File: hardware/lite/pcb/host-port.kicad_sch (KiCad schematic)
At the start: 16 parts, among them J901 1054500101, U901 TPD4E02B04DQAR, U902 TPD4E02B04DQAR, U903 HD3SS3212IRKSR, U904 TPD6S300ARUKR, U905 FUSB302BMPX

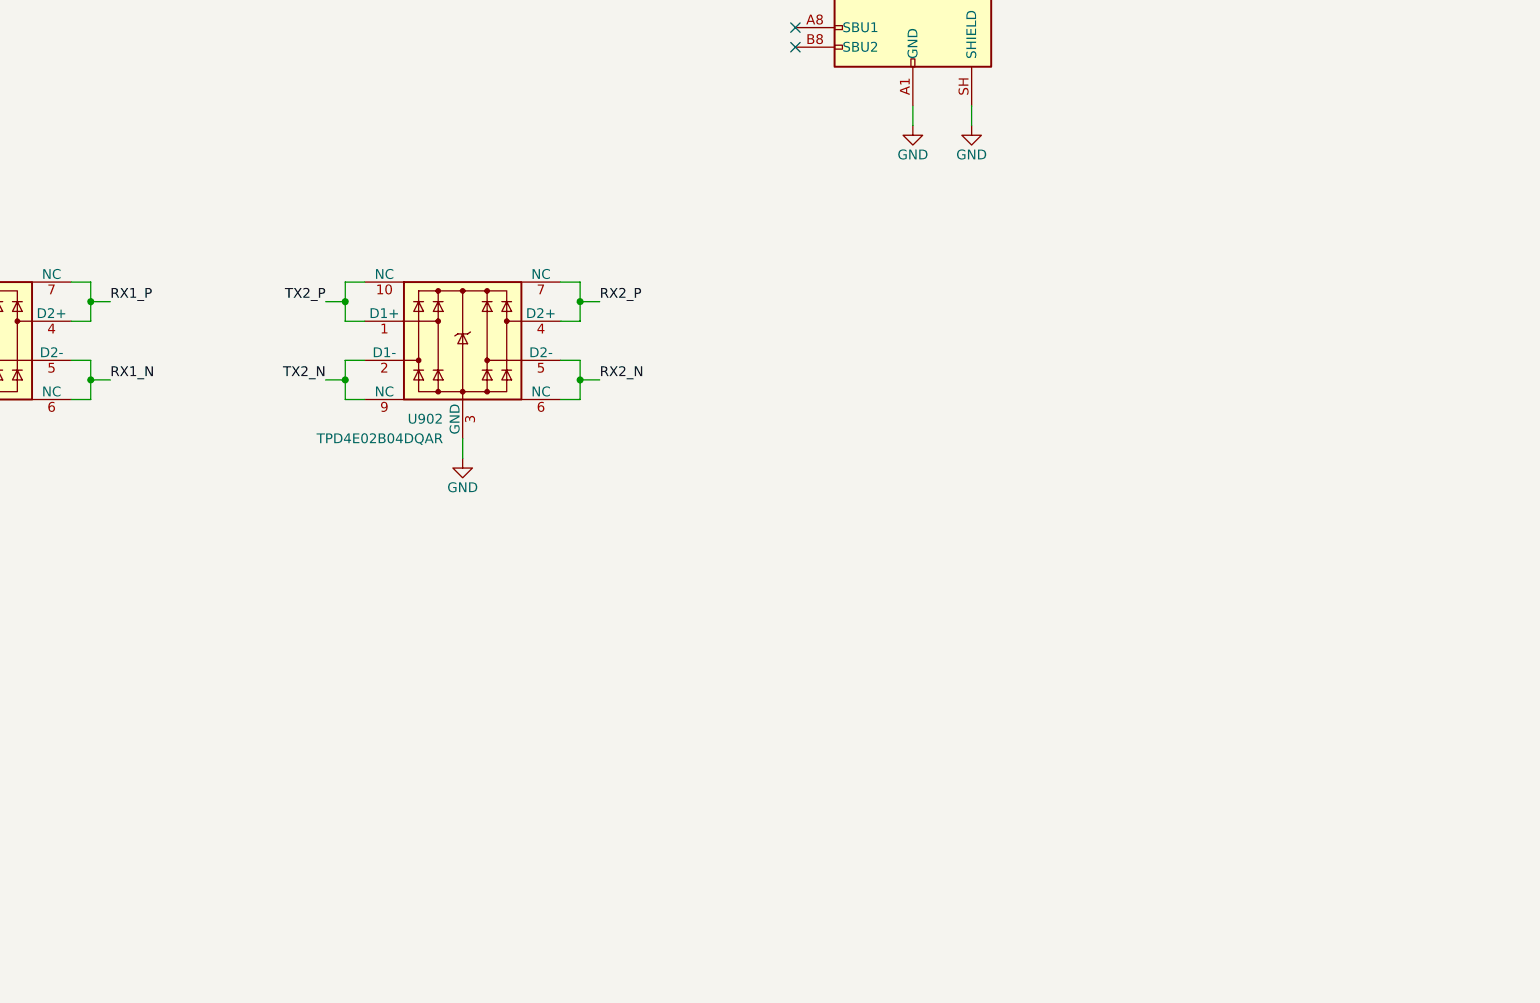
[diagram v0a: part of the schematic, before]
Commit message: feat(hardware): share brick power across ports and add CM5 link
A connected PD supply now runs the logic through its own buck and feeds
one TPS55288 buck-boost stage per port, so the contract is shared as
5-20 V at up to 5 A per port. The hub's VBUS detect becomes an OR gate,
a host-select mux lets a CM5 side board drive the hub over a 24-pin ZIF
link, and a CM5 variant joins Hub and HubPD.

The board is synced to the schematic and its old routing removed; the
new parts wait below the outline for placement.
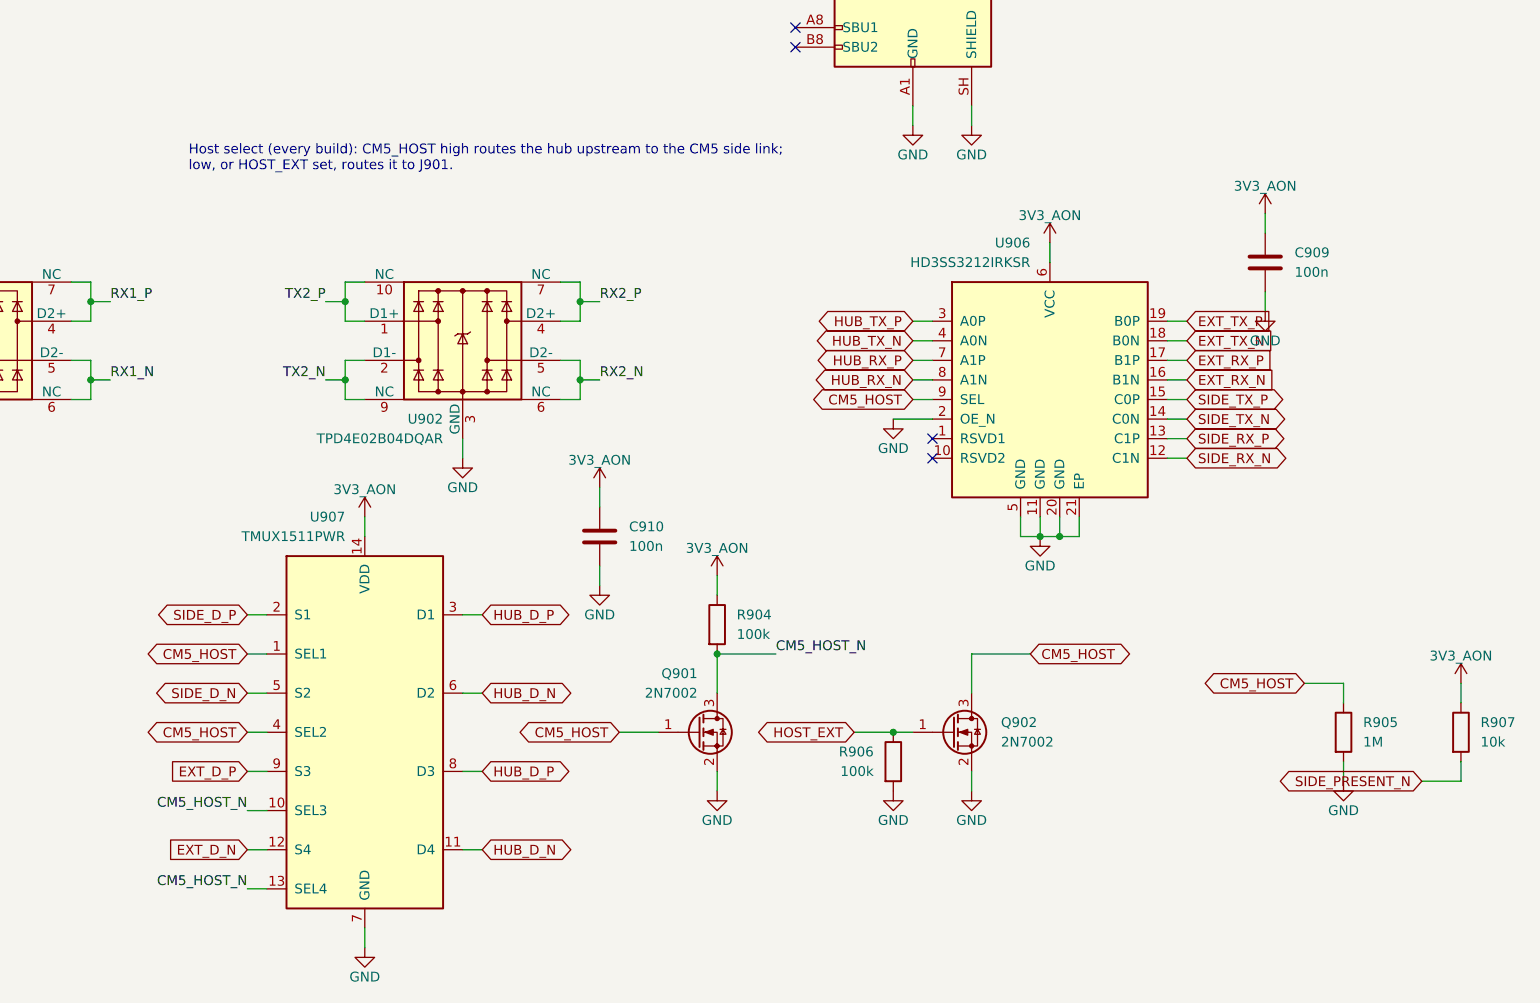
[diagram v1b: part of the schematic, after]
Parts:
- added C909, C910: 100n, Capacitor_SMD:C_0402_1005Metric, symbol Device:C
- added Q901, Q902: 2N7002, Package_TO_SOT_SMD:SOT-23, symbol Transistor_FET:2N7002
- added R904, R906: 100k, Resistor_SMD:R_0402_1005Metric, symbol Device:R
- added R905: 1M, Resistor_SMD:R_0402_1005Metric, symbol Device:R
- added R907: 10k, Resistor_SMD:R_0402_1005Metric, symbol Device:R
- added U906: HD3SS3212IRKSR, Package_DFN_QFN:DHVQFN-20-1EP_2.5x4.5mm_P0.5mm_EP1x3mm, symbol Iasis:HD3SS3212IRKSR
- added U907: TMUX1511PWR, Package_SO:TSSOP-14_4.4x5mm_P0.65mm, symbol Iasis:TMUX1511PWR
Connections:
- net 3V3_AON: now also C909.1, C910.1, R904.1, R907.1, U906.6 (VCC), U907.14 (VDD)
- net EXT_D_N: now also U907.12 (S4)
- net EXT_D_P: now also U907.9 (S3)
- net EXT_RX_N: now also U906.16 (B1N)
- net EXT_RX_P: now also U906.17 (B1P)
- net EXT_TX_N: now also U906.18 (B0N)
- net EXT_TX_P: now also U906.19 (B0P)
- net GND: now also C909.2, C910.2, Q901.2 (S), Q902.2 (S), R905.2, R906.2, U906.11 (GND), U906.2 (OE_N), U906.20 (GND), U906.21 (EP), U906.5 (GND), U907.7 (GND)
- new net CM5_HOST: Q901.1 (G), Q902.3 (D), R905.1, U906.9 (SEL), U907.1 (SEL1), U907.4 (SEL2)
- new net CM5_HOST_N: Q901.3 (D), R904.2, U907.10 (SEL3), U907.13 (SEL4)
- new net HOST_EXT: Q902.1 (G), R906.1
- new net HUB_D_N: U907.11 (D4), U907.6 (D2)
- new net HUB_D_P: U907.3 (D1), U907.8 (D3)
- new net HUB_RX_N: U906.8 (A1N)
- new net HUB_RX_P: U906.7 (A1P)
- new net HUB_TX_N: U906.4 (A0N)
- new net HUB_TX_P: U906.3 (A0P)
- new net SIDE_D_N: U907.5 (S2)
- new net SIDE_D_P: U907.2 (S1)
- new net SIDE_PRESENT_N: R907.2
- new net SIDE_RX_N: U906.12 (C1N)
- new net SIDE_RX_P: U906.13 (C1P)
- new net SIDE_TX_N: U906.14 (C0N)
- new net SIDE_TX_P: U906.15 (C0P)
- no-connect marks 5 -> 7
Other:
- note added: "Host select (every build): CM5_HOST high routes the hub upstream to the CM5 side link; low, or HOST_EXT set, routes it to J901."

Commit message: feat(hardware): use smaller mux, I2C switch, 595 and button packages
The TMUX1511s move to UQFN-16 (RSV), the TCA9548A to VQFN-24 (RGE),
the 74HC595s to TSSOP-16 and the BOOTSEL and RESET buttons to the
Omron B3U, which frees about 300 mm2 of the middle band. The case
button keeps the PTS645.
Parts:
- U907: value TMUX1511PWR -> TMUX1511RSVR; footprint Package_SO:TSSOP-14_4.4x5mm_P0.65mm -> Package_DFN_QFN:UQFN-16_1.8x2.6mm_P0.4mm; symbol Iasis:TMUX1511PWR -> Iasis:TMUX1511RSVR; LCSC C2866750 -> C2673275; MPN TMUX1511PWR -> TMUX1511RSVR
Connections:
- net 3V3_AON: now also U907.16 (VDD); no longer U907.14 (VDD)
- net CM5_HOST_N: now also U907.11 (SEL3), U907.15 (SEL4); no longer U907.10 (SEL3), U907.13 (SEL4)
- net EXT_D_N: now also U907.14 (S4); no longer U907.12 (S4)
- net EXT_D_P: now also U907.10 (S3); no longer U907.9 (S3)
- net GND: now also U907.8 (GND); no longer U907.7 (GND)
- net HUB_D_N: now also U907.13 (D4); no longer U907.11 (D4)
- net HUB_D_P: now also U907.9 (D3); no longer U907.8 (D3)
- no-connect marks 7 -> 9
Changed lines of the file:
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@@
 	)
 	(no_connect
+		(at 266.7 251.46)
+	)
+	(no_connect
+		(at 266.7 210.82)
+	)
+	(no_connect
 		(at 241.3 88.9)
 	)
@@
 	)
 	(symbol
-		(lib_id "Iasis:TMUX1511PWR")
+		(lib_id "Iasis:TMUX1511RSVR")
 		(at 254 231.14 0)
 		(unit 1)
@@
 			)
 		)
-		(property "Value" "TMUX1511PWR"
+		(property "Value" "TMUX1511RSVR"
 			(at 251.46 205.74 0)
 			(show_name no)
@@
 			)
 		)
-		(property "Footprint" "Package_SO:TSSOP-14_4.4x5mm_P0.65mm"
+		(property "Footprint" "Package_DFN_QFN:UQFN-16_1.8x2.6mm_P0.4mm"
 			(at 254 231.14 0)
 			(hide yes)
@@
 			)
 		)
-		(property "LCSC" "C2866750"
+		(property "LCSC" "C2673275"
 			(at 254 231.14 0)
 			(hide yes)
@@
 			)
 		)
-		(property "MPN" "TMUX1511PWR"
+		(property "MPN" "TMUX1511RSVR"
 			(at 254 231.14 0)
 			(hide yes)
@@
 		(pin "6"
 		)
-		(pin "7"
-		)
 		(pin "8"
 		)
@@
 		(pin "11"
 		)
-		(pin "12"
-		)
 		(pin "13"
 		)
 		(pin "14"
 		)
+		(pin "15"
+		)
+		(pin "16"
+		)
+		(pin "7"
+		)
+		(pin "12"
+		)
 		(instances

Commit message: fix(hardware): put the hub and side-link lanes in USB_90
The hub upstream and CM5 side-link nets (HUB_ and SIDE_ TX, RX and D)
were left in the default class when the side link was added. A rule
lets the TMUX1511's corner pads keep their 0.15 mm package spacing
inside the class clearance.

U907 now carries D- on channel 1 and D+ on channel 2, the reverse of
channels 3 and 4, so each HUB_D net joins neighbouring pins around the
RSV package and its four-pin tie needs no via.
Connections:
- net HUB_D_N: now also U907.3 (D1); no longer U907.6 (D2)
- net HUB_D_P: now also U907.6 (D2); no longer U907.3 (D1)
- net SIDE_D_N: now also U907.2 (S1); no longer U907.5 (S2)
- net SIDE_D_P: now also U907.5 (S2); no longer U907.2 (S1)

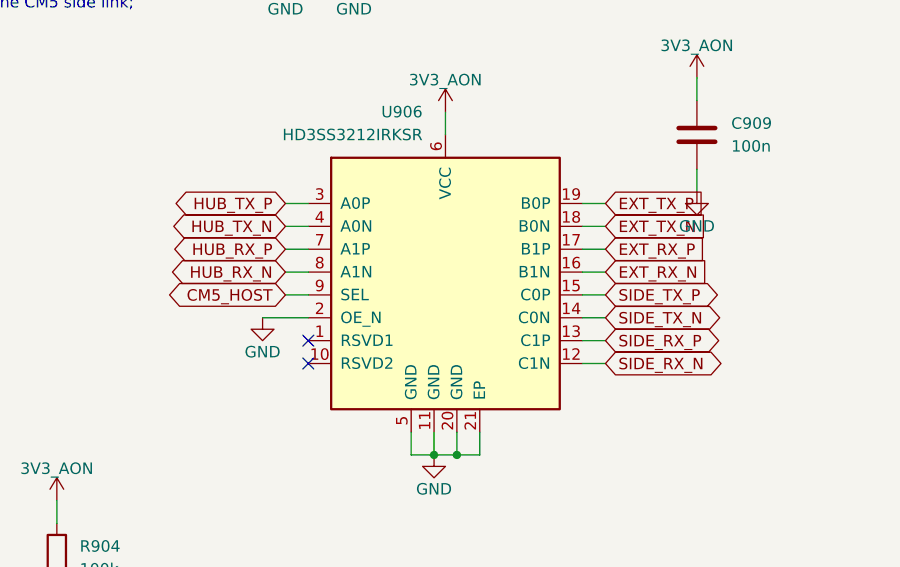
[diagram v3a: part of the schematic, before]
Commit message: fix(hardware): swap the host-select mux channels
The hub's upstream pins read RX before TX, the reverse of the
HD3SS3212's channel order, so U906 now carries RX on channel 0 and TX
on channel 1 at all three ports. The hub and side-link pairs reach it
without crossing; the J901 path keeps the one crossing its pin orders
require, in the run to U903, which stays in step with the target-port
muxes.
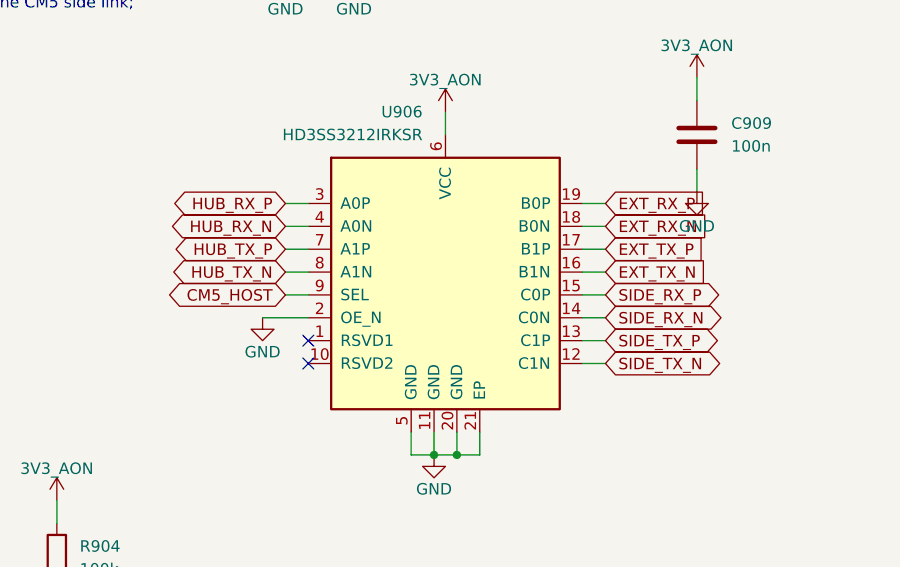
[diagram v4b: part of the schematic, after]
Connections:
- net EXT_RX_N: now also U906.18 (B0N); no longer U906.16 (B1N)
- net EXT_RX_P: now also U906.19 (B0P); no longer U906.17 (B1P)
- net EXT_TX_N: now also U906.16 (B1N); no longer U906.18 (B0N)
- net EXT_TX_P: now also U906.17 (B1P); no longer U906.19 (B0P)
- net HUB_RX_N: now also U906.4 (A0N); no longer U906.8 (A1N)
- net HUB_RX_P: now also U906.3 (A0P); no longer U906.7 (A1P)
- net HUB_TX_N: now also U906.8 (A1N); no longer U906.4 (A0N)
- net HUB_TX_P: now also U906.7 (A1P); no longer U906.3 (A0P)
- net SIDE_RX_N: now also U906.14 (C0N); no longer U906.12 (C1N)
- net SIDE_RX_P: now also U906.15 (C0P); no longer U906.13 (C1P)
- net SIDE_TX_N: now also U906.12 (C1N); no longer U906.14 (C0N)
- net SIDE_TX_P: now also U906.13 (C1P); no longer U906.15 (C0P)

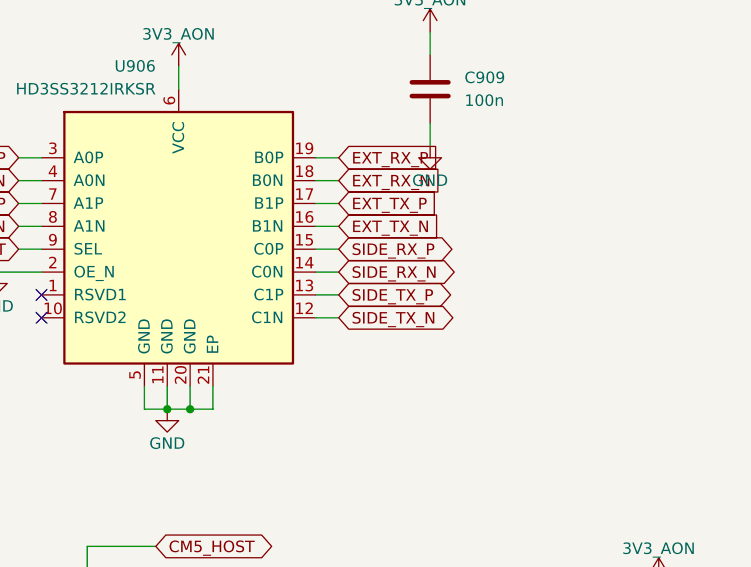
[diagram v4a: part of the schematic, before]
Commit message: fix(hardware): reverse the side-link SuperSpeed polarity at U906
J2001 and U906 both put P on the right of a pair heading in, so a
planar side-link pair lands P/N reversed. U906 takes the reversal on
both SIDE pairs and the receivers correct SuperSpeed polarity; J2001
keeps the side board's pinout.
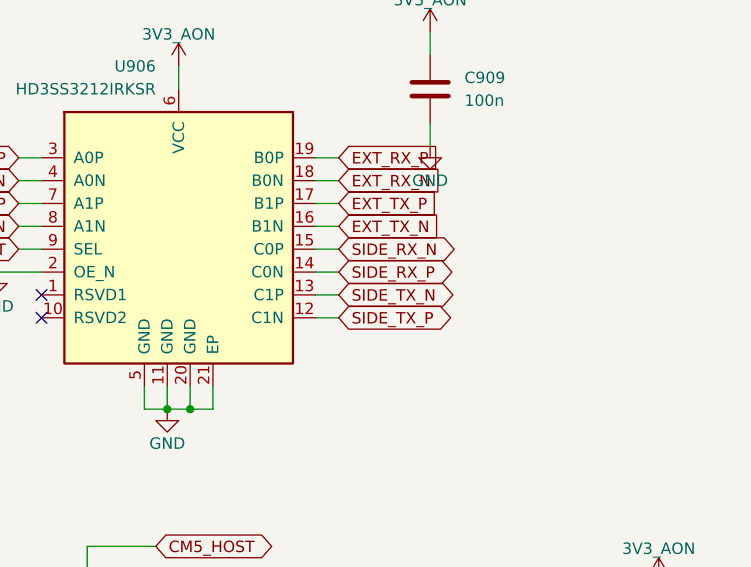
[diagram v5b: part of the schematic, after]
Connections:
- net SIDE_RX_N: now also U906.15 (C0P); no longer U906.14 (C0N)
- net SIDE_RX_P: now also U906.14 (C0N); no longer U906.15 (C0P)
- net SIDE_TX_N: now also U906.13 (C1P); no longer U906.12 (C1N)
- net SIDE_TX_P: now also U906.12 (C1N); no longer U906.13 (C1P)

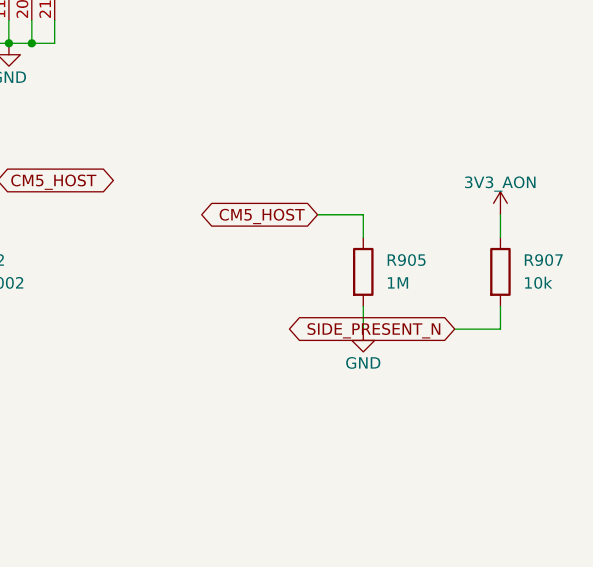
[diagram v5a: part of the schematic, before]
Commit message: feat(pcb): place pooled power blocks
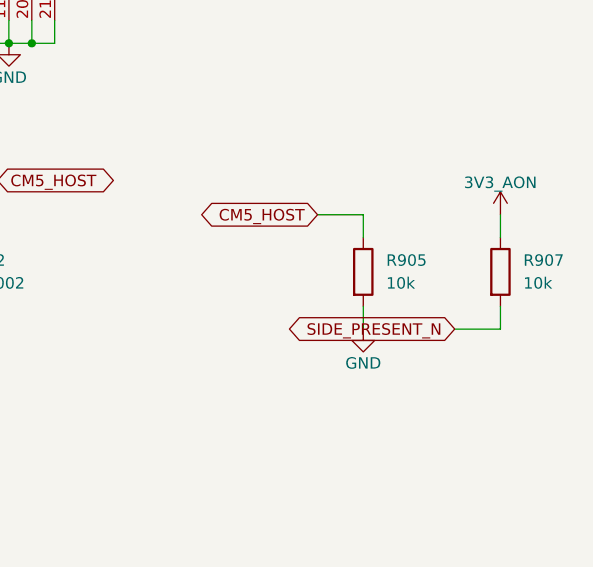
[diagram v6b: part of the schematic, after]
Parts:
- R905: value 1M -> 10k; LCSC C26083 -> C25744; MPN 0402WGF1004TCE -> 0402WGF1002TCE
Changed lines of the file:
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@@
 			)
 		)
-		(property "Value" "1M"
+		(property "Value" "10k"
 			(at 383.54 232.41 0)
 			(show_name no)
@@
 			)
 		)
-		(property "Datasheet" "https://www.lcsc.com/datasheet/lcsc_datasheet_2206010100_UNI-ROYAL-Uniroyal-Elec-0402WGF1003TCE_C25741.pdf"
+		(property "Datasheet" "https://www.lcsc.com/datasheet/lcsc_datasheet_2411221126_UNI-ROYAL-Uniroyal-Elec-0402WGF1002TCE_C25744.pdf"
 			(at 381 231.14 0)
 			(hide yes)
@@
 			)
 		)
-		(property "LCSC" "C26083"
+		(property "LCSC" "C25744"
 			(at 381 231.14 0)
 			(hide yes)
@@
 			)
 		)
-		(property "MPN" "0402WGF1004TCE"
+		(property "MPN" "0402WGF1002TCE"
 			(at 381 231.14 0)
 			(hide yes)
